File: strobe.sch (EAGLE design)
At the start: 38 parts, among them IC1 AT90USB162A, Q1 IRF3704S, Q2 IRF3704S, T5 BC849, T6 BC849

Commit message: Poprawki Schematów
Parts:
- C4, C5: device rcl:C-EUC0805 -> rcl:C-EUC0603
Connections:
- net GND: now also C1.2, C4.2, C5.2
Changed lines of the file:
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@@
 <part name="GND10" library="SparkFun-Aesthetics" deviceset="GND" device=""/>
 <part name="Q3" library="crystal" deviceset="CRYSTAL" device="SM49"/>
-<part name="C4" library="rcl" deviceset="C-EU" device="C0805" value="22Pf"/>
-<part name="C5" library="rcl" deviceset="C-EU" device="C0805" value="22Pf"/>
+<part name="C4" library="rcl" deviceset="C-EU" device="C0603" value="22Pf"/>
+<part name="C5" library="rcl" deviceset="C-EU" device="C0603" value="22Pf"/>
 <part name="GND7" library="SparkFun-Aesthetics" deviceset="GND" device=""/>
 <part name="R8" library="rcl" deviceset="R-EU_" device="R0805" value="10K"/>
@@
 </segment>
 <segment>
-<wire x1="2.54" y1="144.78" x2="0" y2="144.78" width="0.1524" layer="91"/>
+<wire x1="2.54" y1="144.78" x2="2.286" y2="144.78" width="0.1524" layer="91"/>
+<wire x1="2.286" y1="144.78" x2="0" y2="144.78" width="0.1524" layer="91"/>
 <wire x1="0" y1="144.78" x2="0" y2="137.16" width="0.1524" layer="91"/>
 <wire x1="0" y1="137.16" x2="0" y2="132.08" width="0.1524" layer="91"/>
-<wire x1="2.54" y1="137.16" x2="0" y2="137.16" width="0.1524" layer="91"/>
-<wire x1="5.08" y1="154.94" x2="0" y2="154.94" width="0.1524" layer="91"/>
+<wire x1="2.54" y1="137.16" x2="2.286" y2="137.16" width="0.1524" layer="91"/>
+<wire x1="2.286" y1="137.16" x2="0" y2="137.16" width="0.1524" layer="91"/>
+<wire x1="5.08" y1="154.94" x2="4.826" y2="154.94" width="0.1524" layer="91"/>
+<wire x1="4.826" y1="154.94" x2="0" y2="154.94" width="0.1524" layer="91"/>
 <wire x1="0" y1="154.94" x2="0" y2="144.78" width="0.1524" layer="91"/>
 <junction x="0" y="144.78"/>
 <junction x="0" y="137.16"/>
 <pinref part="GND7" gate="1" pin="GND"/>
+<pinref part="C5" gate="G$1" pin="2"/>
+<junction x="2.286" y="137.16"/>
+<pinref part="C4" gate="G$1" pin="2"/>
+<junction x="2.286" y="144.78"/>
+<pinref part="C1" gate="G$1" pin="2"/>
+<junction x="4.826" y="154.94"/>
 </segment>
 <segment>

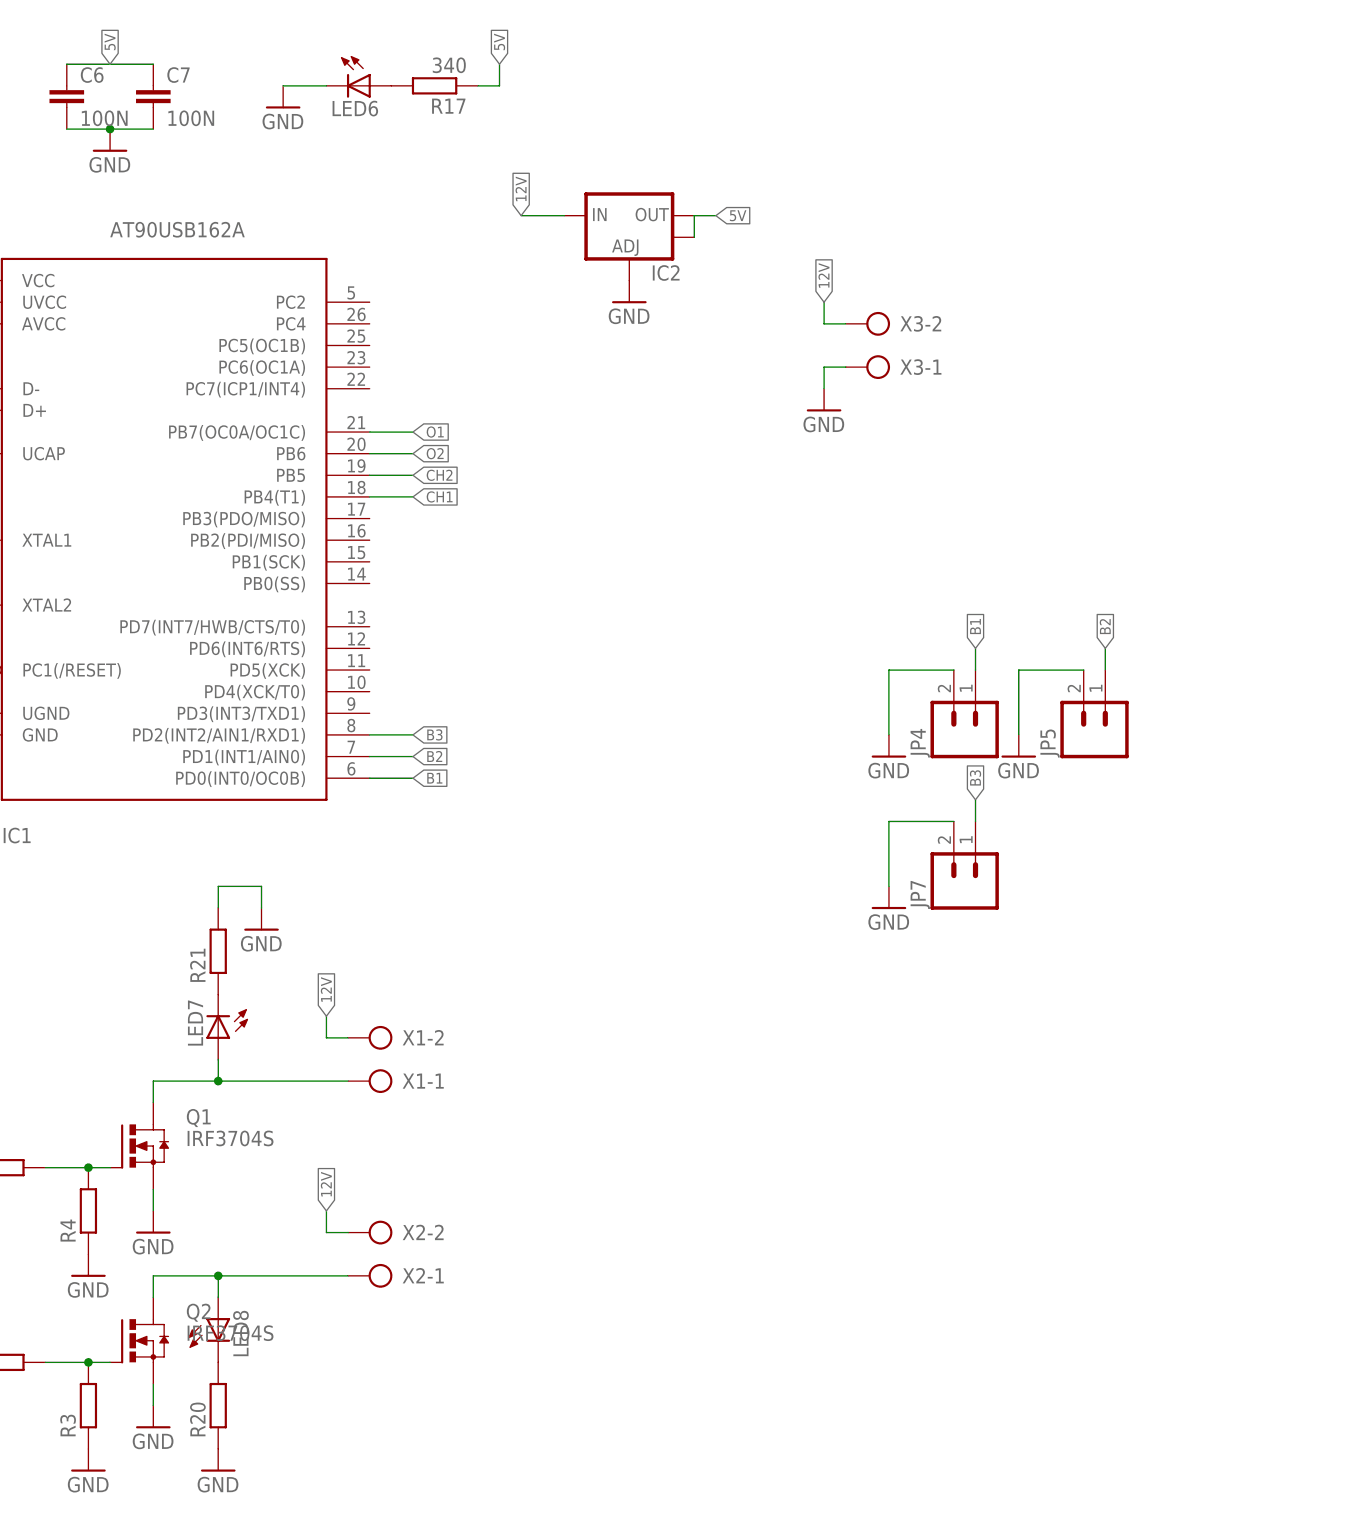
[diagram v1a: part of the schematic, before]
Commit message: Nowa płytka
4 lampy + RJ45
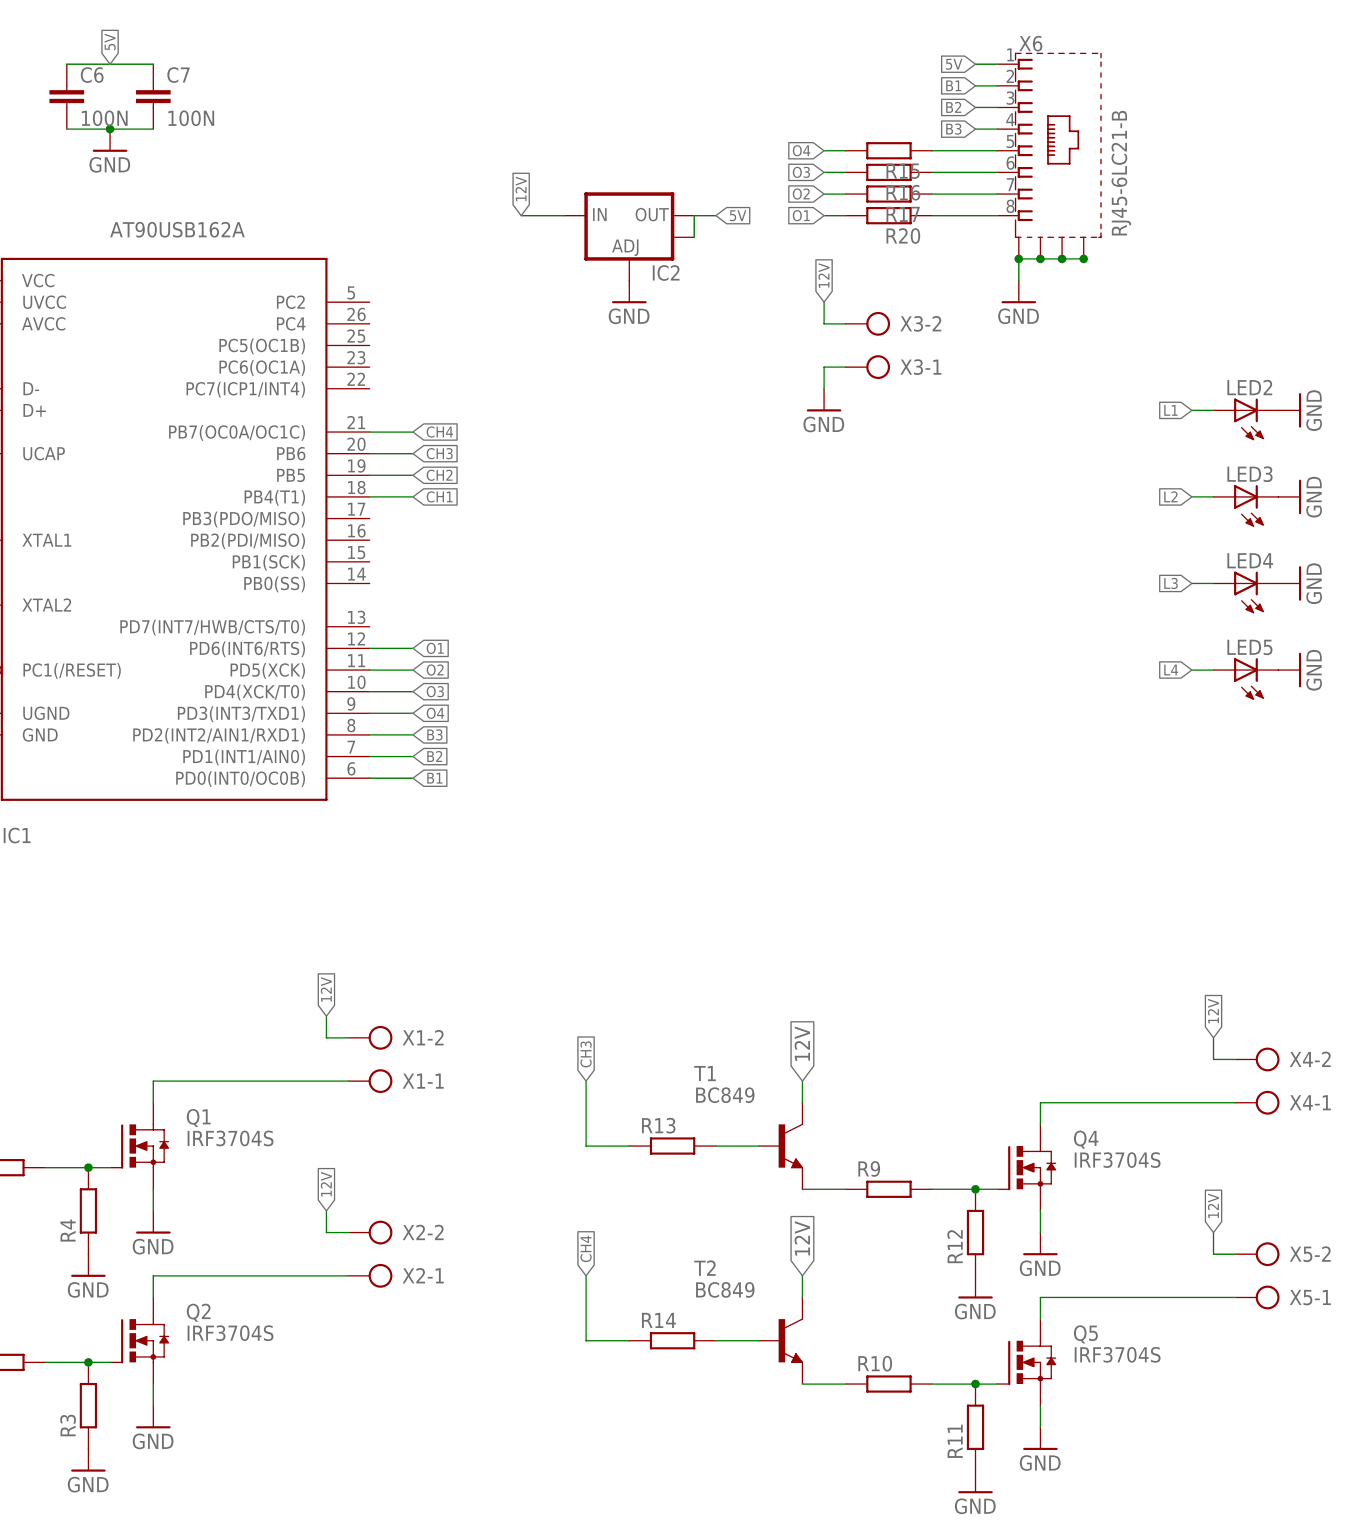
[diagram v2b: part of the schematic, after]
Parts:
- removed JP4, JP5, JP7: (no value), SparkFun-Connectors:M02PTH3
- removed LED6, LED7, LED8: (no value), led:LEDSML0805
- removed R21: (no value), rcl:R-EU_R0805
- added LED2, LED3, LED4, LED5: (no value), led:LEDSML0805
- added Q4, Q5: IRF3704S, transistor-power:IRF3704S
- added R10, R11, R12, R13, R14, R15, R16, R9: (no value), rcl:R-EU_R0805
- added T1, T2: BC849, transistor:BC849
- added X4, X5: (no value), con-ptr500:AK300/2
- added X6: RJ45-6LC21-B, con-tycoelectronics:RJ45-6LC21-B
- R17: value 340 -> (none)
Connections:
- removed net N$27: LED6.A, R17.2
- removed net N$32: LED8.C, R20.2
- removed net N$33: LED7.C, R21.1
- new net CH3: IC1.PB6, R13.1
- new net CH4: IC1.PB7(OC0A/OC1C), R14.1
- new net L1: LED2.A, R20.1, X6.8
- new net L2: LED3.A, R17.1, X6.7
- new net L3: LED4.A, R16.1, X6.6
- new net L4: LED5.A, R15.1, X6.5
- new net N$11: Q4.G, R12.2, R9.2
- new net N$15: Q5.G, R10.2, R11.2
- new net N$16: Q4.D, X4-1.KL
- new net N$17: Q5.D, X5-1.KL
- new net N$18: R9.1, T1.E
- new net N$19: R10.1, T2.E
- new net N$20: R13.2, T1.B
- new net N$21: R14.2, T2.B
- new net O3: IC1.PD4(XCK/T0), R16.2
- new net O4: IC1.PD3(INT3/TXD1), R15.2
- net 12V: now also T1.C, T2.C, X4-2.KL, X5-2.KL
- net 5V: now also X6.1; no longer R17.1
- net B1: now also X6.2; no longer JP4.1
- net B2: now also X6.3; no longer JP5.1
- net B3: now also X6.4; no longer JP7.1
- net GND: now also LED2.C, LED3.C, LED4.C, LED5.C, Q4.S, Q5.S, R11.1, R12.1, X6.S@1, X6.S@2, X6.S@3, X6.S@4; no longer JP4.2, JP5.2, JP7.2, LED6.C, R20.1, R21.2
- net N$3: no longer LED7.A
- net N$4: no longer LED8.A
- net O1: now also IC1.PD6(INT6/RTS), R20.2; no longer IC1.PB7(OC0A/OC1C)
- net O2: now also IC1.PD5(XCK), R17.2; no longer IC1.PB6
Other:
- moved on the sheet: R17, R20

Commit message: board fix
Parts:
- added C8, C9: 100N, rcl:C-EUC0805
- added D1: (no value), diode:DIODE-SMB
- added LED6: (no value), led:LEDSML0805
- added R21: 340, rcl:R-EU_R0805
- added R22, R24, R26, R28: (no value), rcl:R-EU_R0805
- added T3, T4, T7, T8: BC849, transistor:BC849
- added TP1, TP2, TP3, TP4: TPB1,27, testpad:TPB1,27
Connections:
- new net N$22: IC1.PB3(PDO/MISO), TP1.TP
- new net N$23: LED6.A, R21.2
- new net N$24: R22.2, T3.B
- new net N$25: IC1.PB2(PDI/MISO), TP2.TP
- new net N$27: R24.2, T4.B
- new net N$32: IC1.PB1(SCK), TP3.TP
- new net N$34: R26.2, T7.B
- new net N$37: R28.2, T8.B
- new net T1: IC1.PD6(INT6/RTS), R22.1
- new net T2: IC1.PD5(XCK), R24.1
- new net T3: IC1.PD4(XCK/T0), R26.1
- new net T4: IC1.PD3(INT3/TXD1), R28.1
- net 12V: now also C8.1, D1.C, R21.1
- net 5V: now also C9.1, D1.A, T3.C, T4.C, T7.C, T8.C
- net GND: now also C8.2, C9.2, LED6.C
- net N$14: now also TP4.TP
- net O1: now also T3.E; no longer IC1.PD6(INT6/RTS)
- net O2: now also T4.E; no longer IC1.PD5(XCK)
- net O3: now also T7.E; no longer IC1.PD4(XCK/T0)
- net O4: now also T8.E; no longer IC1.PD3(INT3/TXD1)

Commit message: PCB extreme makeover
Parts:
- removed D1: (no value), diode:DIODE-SMB
- removed LED2, LED3, LED4, LED5: (no value), led:LEDSML0805
- removed X6: RJ45-6LC21-B, con-tycoelectronics:RJ45-6LC21-B
- added R23, R25, R27: (no value), rcl:R-EU_R0805
- added T9: BC849, transistor:BC849
- added U$1: RJ45, RJ45:RJ45
- JP1: value USBSMD -> USB-B; device SparkFun-Connectors:USBSMD -> SparkFun-Connectors:USBPTH
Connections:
- removed net L1: LED2.A, R20.1, X6.8
- removed net L2: LED3.A, R17.1, X6.7
- removed net L3: LED4.A, R16.1, X6.6
- removed net L4: LED5.A, R15.1, X6.5
- new net N$26: R25.1, U$1.LED1+
- new net N$33: R15.2, U$1.5
- new net N$35: R16.2, U$1.6
- new net N$36: R17.2, U$1.7
- new net N$38: R20.2, U$1.8
- new net N$39: R23.2, T9.B
- new net N$40: R27.1, U$1.LED2+
- new net O5: R25.2, T9.E
- new net T5: IC1.PC2, R23.1
- net 12V: no longer D1.C
- net 5V: now also R27.2, T9.C, U$1.1; no longer D1.A, X6.1
- net B1: now also U$1.2; no longer X6.2
- net B2: now also U$1.3; no longer X6.3
- net B3: now also U$1.4; no longer X6.4
- net GND: now also U$1.LED1-, U$1.LED2-; no longer LED2.C, LED3.C, LED4.C, LED5.C, X6.S@1, X6.S@2, X6.S@3, X6.S@4
- net O1: now also R20.1; no longer R20.2
- net O2: now also R17.1; no longer R17.2
- net O3: now also R16.1; no longer R16.2
- net O4: now also R15.1; no longer R15.2
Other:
- moved on the sheet: R15, R16, R17, R20, R22, R24, R26, R28, T3, T4, T7, T8

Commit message: Close-to-final version of board
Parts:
- removed R23, R25, R27: (no value), rcl:R-EU_R0805
- removed T9: BC849, transistor:BC849
- removed X1, X2, X3, X4, X5: (no value), con-ptr500:AK300/2
- added F1: FUSEX20MM, SparkFun-Passives:FUSEX20MM
- added X6: D-SUB9-H3M09RA, con-thomas-betts:D-SUB9-H3M09RA
- U$1: value RJ45 -> MF42-10; device RJ45:RJ45 -> con-amphenol:MF42-10
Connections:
- removed net N$16: Q4.D, X4-1.KL
- removed net N$17: Q5.D, X5-1.KL
- removed net N$38: R20.2, U$1.8
- removed net N$39: R23.2, T9.B
- removed net N$4: Q2.D, X2-1.KL
- removed net N$40: R27.1, U$1.LED2+
- removed net O5: R25.2, T9.E
- new net L1: Q1.D, U$1.6
- new net L2: Q2.D, U$1.9
- new net L3: Q4.D, U$1.7
- new net L4: Q5.D, U$1.10
- net 12V: now also F1.1, U$1.2, U$1.3, U$1.4, U$1.5; no longer X1-2.KL, X2-2.KL, X3-2.KL, X4-2.KL, X5-2.KL
- net 5V: now also X6-9.F; no longer R27.2, T9.C, U$1.1
- net B1: now also X6-4.F; no longer U$1.2
- net B2: now also X6-8.F; no longer U$1.3
- net B3: now also X6-3.F; no longer U$1.4
- net GND: now also U$1.11, U$1.12, U$1.8, X6-5.F; no longer U$1.LED1-, U$1.LED2-, X3-1.KL
- net N$26: now also R20.2, X6-1.F; no longer R25.1, U$1.LED1+
- net N$3: now also F1.2, U$1.1; no longer Q1.D, X1-1.KL
- net N$33: now also R17.2, X6-6.F; no longer R15.2, U$1.5
- net N$35: now also X6-2.F; no longer U$1.6
- net N$36: now also R15.2, X6-7.F; no longer R17.2, U$1.7
- net T5: no longer R23.1
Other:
- moved on the sheet: R15, R16, R17, R20
